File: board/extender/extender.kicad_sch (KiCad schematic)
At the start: 3 parts, among them J1 EDAC 395-040-559-212, J2 Pin Header, P1 Card Edge

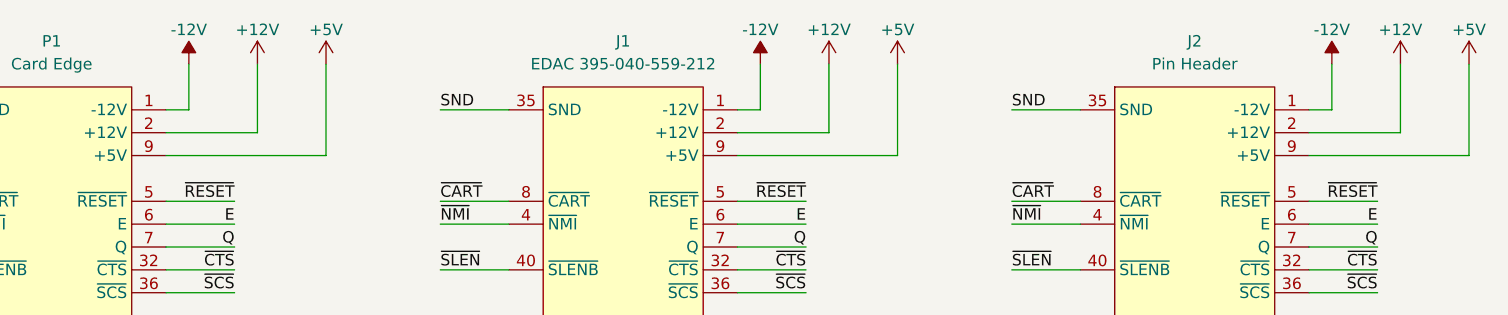
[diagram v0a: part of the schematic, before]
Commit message: Update KiCad projects to v8.
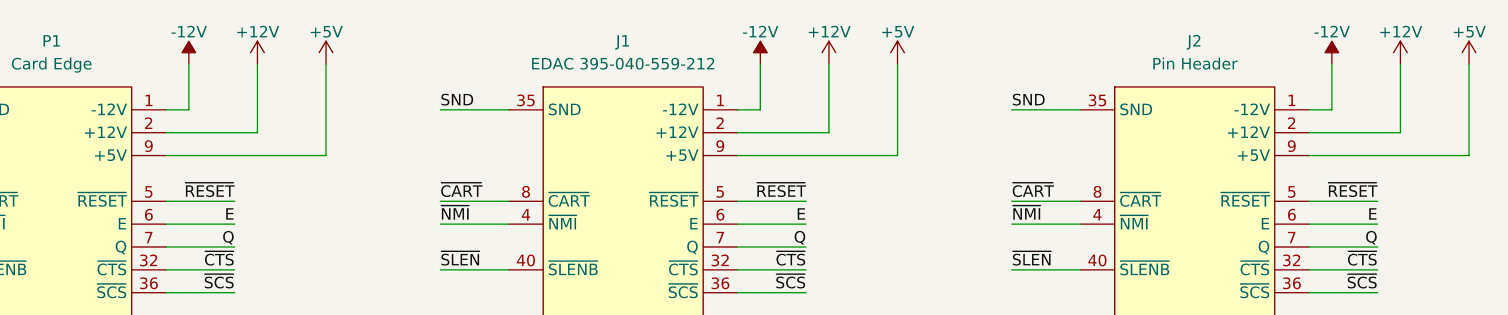
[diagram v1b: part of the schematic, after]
